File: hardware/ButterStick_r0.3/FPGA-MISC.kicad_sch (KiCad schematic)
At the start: 5 parts, among them U4 ECP5UM5G_85_CABGA381, X1 ASDMB

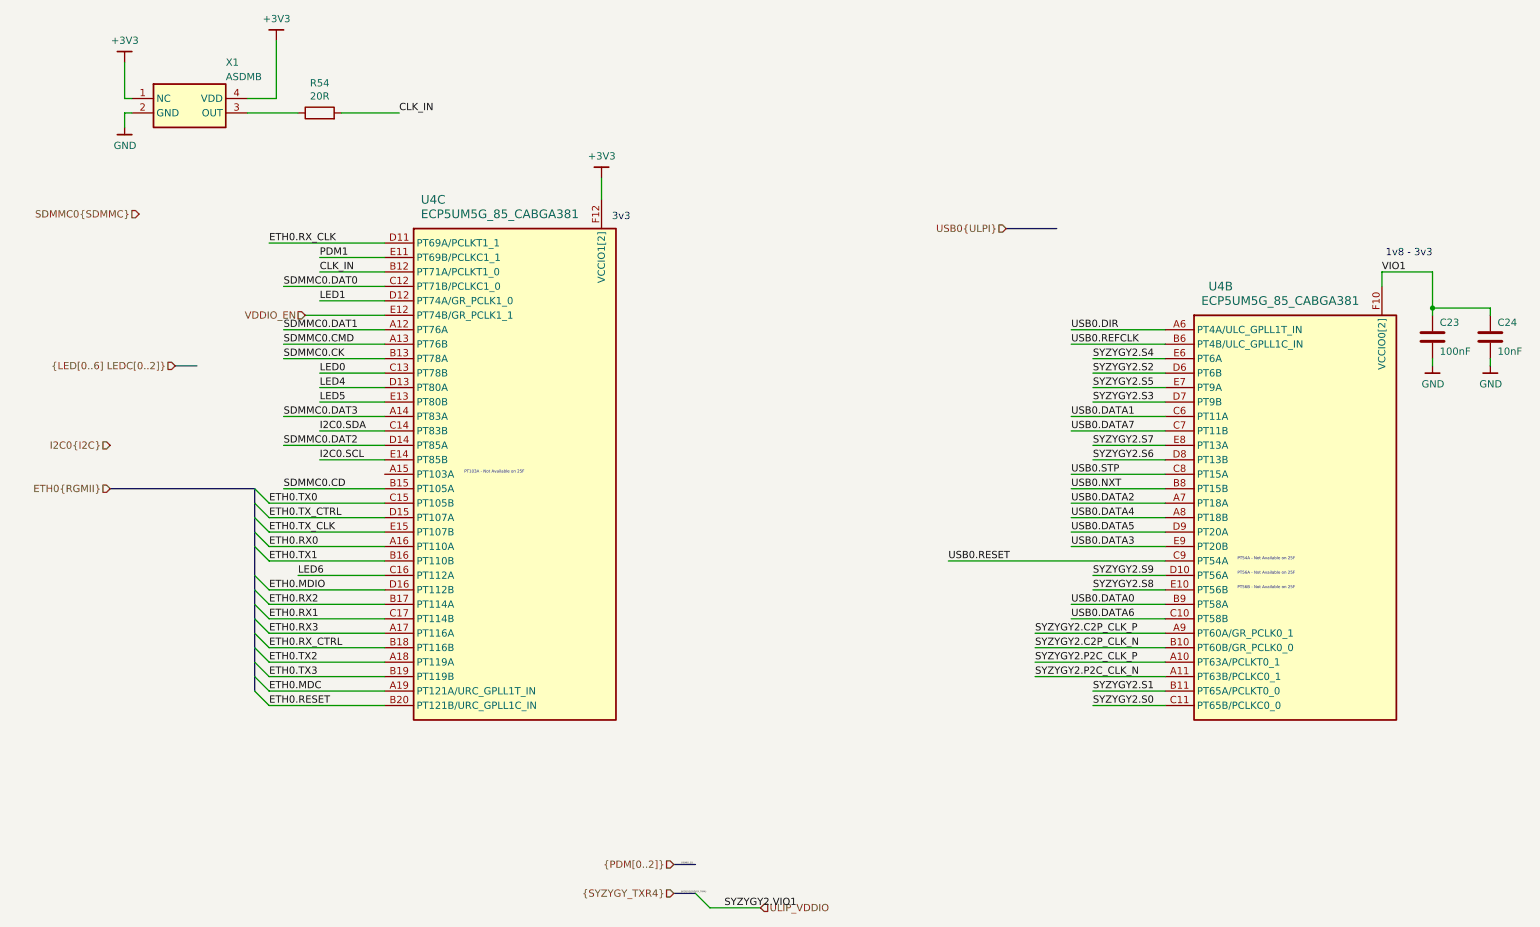
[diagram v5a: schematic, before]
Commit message: hw.r0d3: Fix ULPI VCCIO
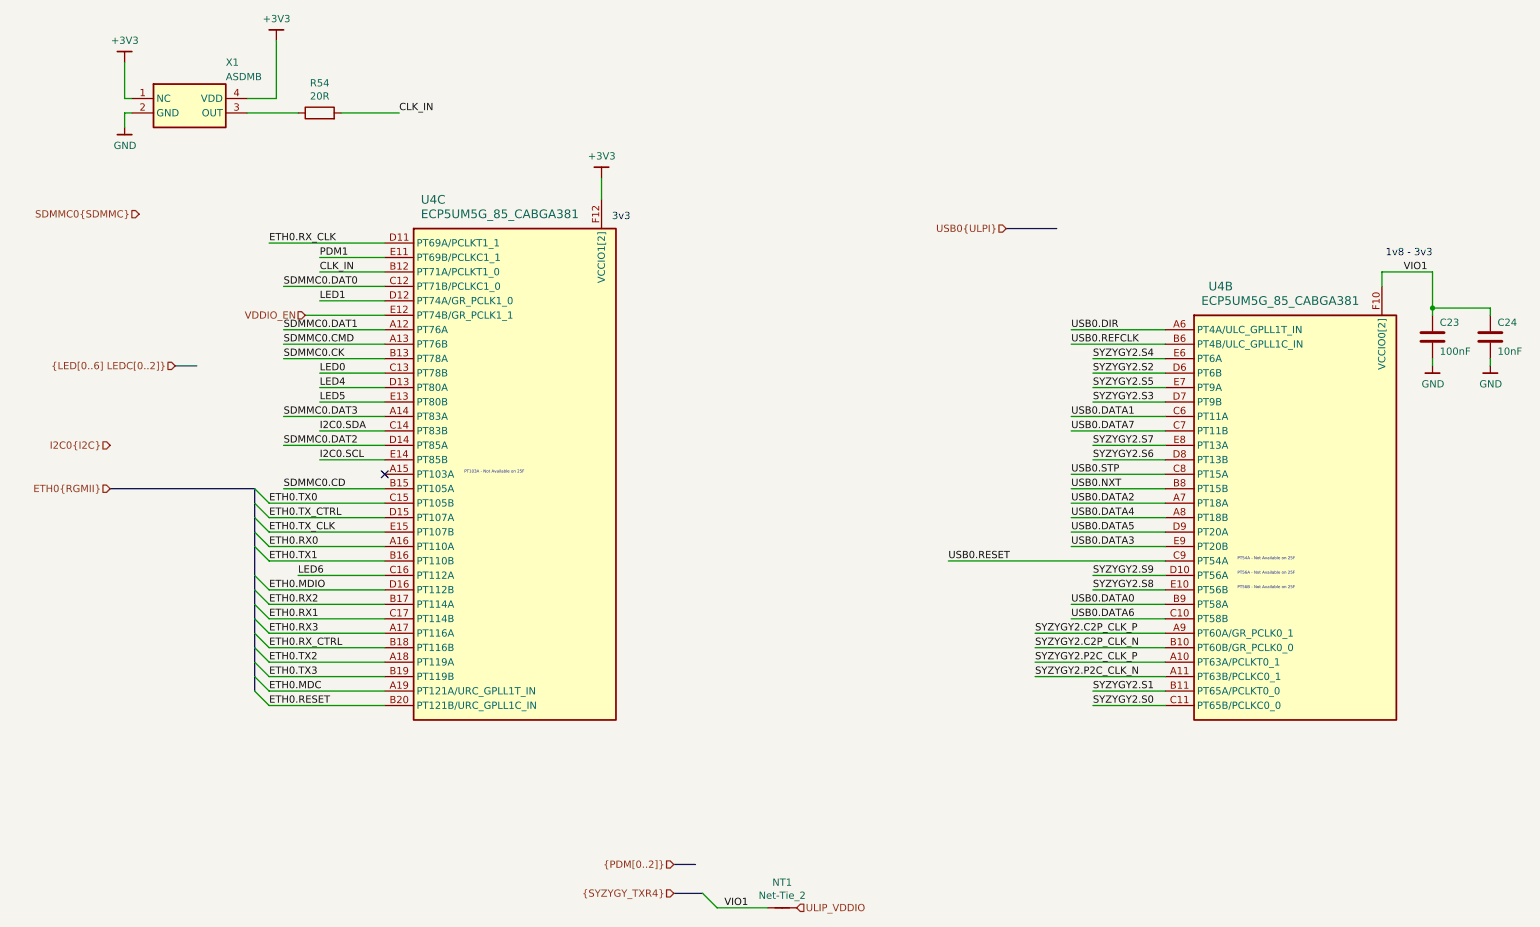
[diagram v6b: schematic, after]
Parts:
- added NT1: Net-Tie_2, NetTie:NetTie-2_SMD_Pad0.5mm, symbol Device:Net-Tie_2
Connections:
- net ULIP_VDDIO: now also NT1.2
- net VIO1: now also NT1.1
- no-connect marks 0 -> 1
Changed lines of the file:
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@@
   (paper "A4")
   (junction (at 261.62 78.74) (diameter 0) (color 0 0 0 0))
+  (no_connect (at 77.47 107.95))
   (bus_entry (at 57.15 113.03) (size -2.54 -2.54)
     (stroke (width 0.1524) (type solid) (color 0 0 0 0))
@@
     (stroke (width 0.1524) (type solid) (color 0 0 0 0))
   )
-  (bus_entry (at 132.08 181.61) (size 2.54 2.54)
+  (bus_entry (at 133.35 181.61) (size 2.54 2.54)
     (stroke (width 0.1524) (type solid) (color 0 0 0 0))
   )
@@
     (stroke (width 0) (type solid) (color 0 0 0 0))
   )
-  (wire (pts (xy 134.62 184.15) (xy 143.51 184.15))
+  (wire (pts (xy 135.89 184.15) (xy 144.78 184.15))
     (stroke (width 0) (type solid) (color 0 0 0 0))
   )
@@
     (stroke (width 0) (type solid) (color 0 0 0 0))
   )
-  (bus (pts (xy 54.61 110.49) (xy 54.61 113.03))
-    (stroke (width 0) (type solid) (color 0 0 0 0))
-  )
-  (bus (pts (xy 54.61 113.03) (xy 54.61 118.11))
-    (stroke (width 0) (type solid) (color 0 0 0 0))
-  )
-  (bus (pts (xy 54.61 118.11) (xy 54.61 120.65))
-    (stroke (width 0) (type solid) (color 0 0 0 0))
-  )
-  (bus (pts (xy 54.61 120.65) (xy 54.61 128.27))
+  (bus (pts (xy 54.61 110.49) (xy 54.61 115.57))
+    (stroke (width 0) (type solid) (color 0 0 0 0))
+  )
+  (bus (pts (xy 54.61 115.57) (xy 54.61 118.11))
+    (stroke (width 0) (type solid) (color 0 0 0 0))
+  )
+  (bus (pts (xy 54.61 118.11) (xy 54.61 125.73))
+    (stroke (width 0) (type solid) (color 0 0 0 0))
+  )
+  (bus (pts (xy 54.61 125.73) (xy 54.61 128.27))
     (stroke (width 0) (type solid) (color 0 0 0 0))
   )
@@
     (stroke (width 0) (type solid) (color 0 0 0 0))
   )
-  (bus (pts (xy 128.27 181.61) (xy 132.08 181.61))
+  (bus (pts (xy 128.27 181.61) (xy 133.35 181.61))
     (stroke (width 0) (type solid) (color 0 0 0 0))
   )
@@
     (effects (font (size 1.27 1.27)) (justify left bottom))
   )
-  (label "{PDM[0..2]}" (at 129.54 176.53 0)
-    (effects (font (size 0.254 0.254)) (justify left bottom))
-  )
-  (label "SYZYGY2{SYZYGY_TXR4}" (at 129.54 181.61 0)
-    (effects (font (size 0.254 0.254)) (justify left bottom))
-  )
-  (label "SYZYGY2.VIO1" (at 137.16 184.15 0)
+  (label "VIO1" (at 137.16 184.15 0)
     (effects (font (size 1.27 1.27)) (justify left bottom))
   )
@@
     (effects (font (size 1.27 1.27)) (justify left bottom))
   )
-  (label "VIO1" (at 252.73 72.39 0)
+  (label "VIO1" (at 256.54 72.39 0)
     (effects (font (size 1.27 1.27)) (justify left bottom))
   )
@@
     (effects (font (size 1.27 1.27)) (justify right))
   )
-  (hierarchical_label "ULIP_VDDIO" (shape input) (at 143.51 184.15 0)
+  (hierarchical_label "ULIP_VDDIO" (shape input) (at 149.86 184.15 0)
     (effects (font (size 1.27 1.27)) (justify left))
   )
@@
     (effects (font (size 1.27 1.27)) (justify right))
   )
+  (symbol (lib_id "Device:Net-Tie_2") (at 147.32 184.15 0) (unit 1)
+    (in_bom yes) (on_board yes)
+    (property "Reference" "NT1" (id 0) (at 147.32 179.6858 0))
+    (property "Value" "Net-Tie_2" (id 1) (at 147.32 181.9845 0))
+    (property "Footprint" "NetTie:NetTie-2_SMD_Pad0.5mm" (id 2) (at 147.32 184.15 0)
+      (effects (font (size 1.27 1.27)) hide)
+    )
+    (property "Datasheet" "~" (id 3) (at 147.32 184.15 0)
+      (effects (font (size 1.27 1.27)) hide)
+    )
+  )
   (symbol (lib_id "gkl_power:GND") (at 31.75 46.99 0) (unit 1)

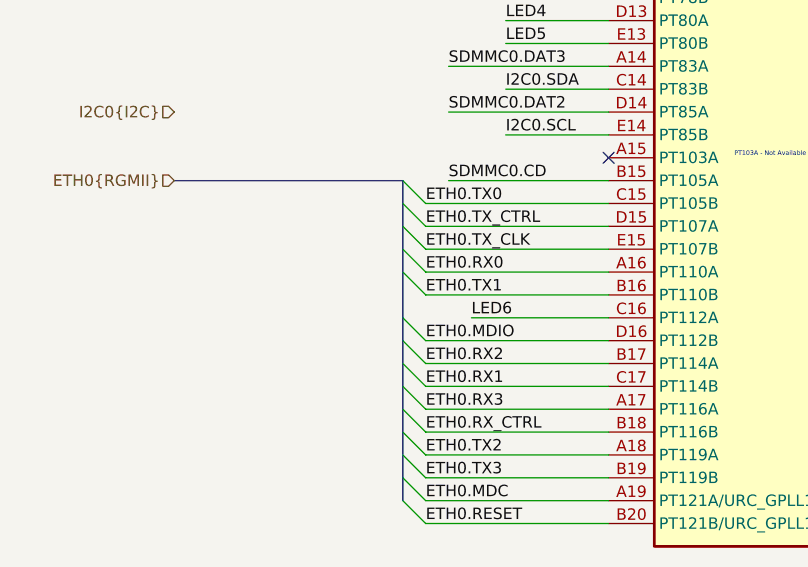
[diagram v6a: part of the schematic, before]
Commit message: hw.r0d3: Remove inverted SYZYGY pairs.
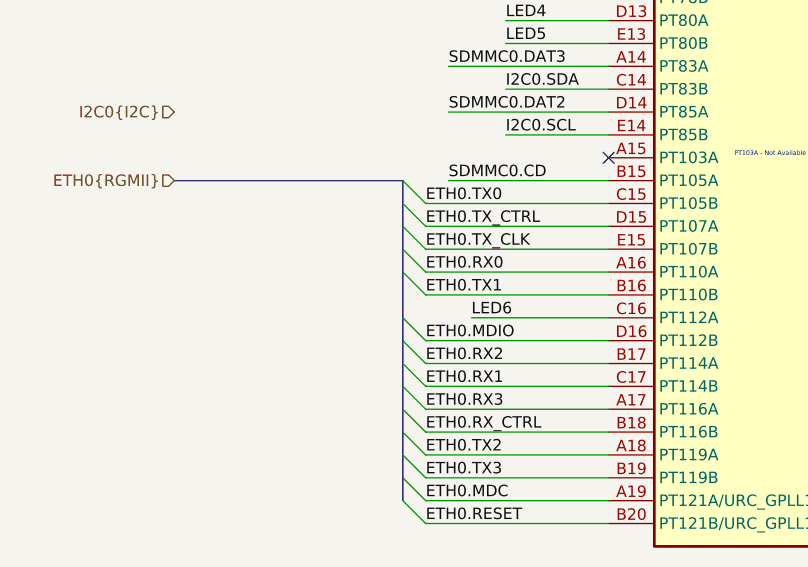
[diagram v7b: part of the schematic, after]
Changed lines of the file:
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@@
 (kicad_sch (version 20200618) (host eeschema "5.99.0-unknown-73168a9~101~ubuntu18.04.1")
-  (page 6 18)
+  (page 1 18)
   (paper "A4")
   (junction (at 261.62 78.74) (diameter 0) (color 0 0 0 0))
@@
     (stroke (width 0) (type solid) (color 0 0 0 0))
   )
-  (bus (pts (xy 54.61 115.57) (xy 54.61 118.11))
-    (stroke (width 0) (type solid) (color 0 0 0 0))
-  )
-  (bus (pts (xy 54.61 118.11) (xy 54.61 125.73))
-    (stroke (width 0) (type solid) (color 0 0 0 0))
-  )
-  (bus (pts (xy 54.61 125.73) (xy 54.61 128.27))
-    (stroke (width 0) (type solid) (color 0 0 0 0))
-  )
+  (bus (pts (xy 54.61 115.57) (xy 54.61 120.65))
+    (stroke (width 0) (type solid) (color 0 0 0 0))
+  )
+  (bus (pts (xy 54.61 120.65) (xy 54.61 128.27))
+    (stroke (width 0) (type solid) (color 0 0 0 0))
+  )
